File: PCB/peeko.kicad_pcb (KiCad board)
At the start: 2 copper layers, 21.8 x 51.3 mm, 6 parts, among them J1 Rasberry PI Pico, J2 Conn_02x15_Odd_Even, J3 Conn_01x02_Pin, J4 Conn_01x02_Pin

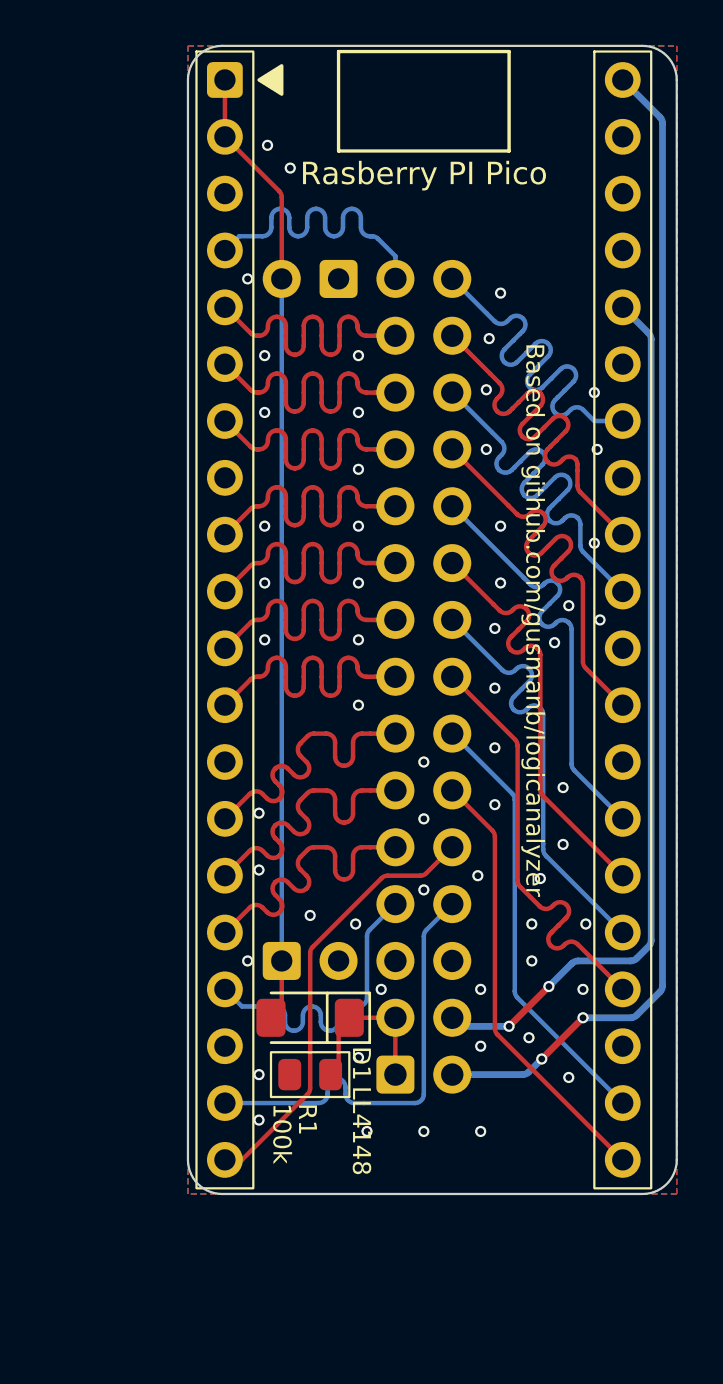
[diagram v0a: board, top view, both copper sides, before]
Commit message: schematic for JY board, remove all but PCBs
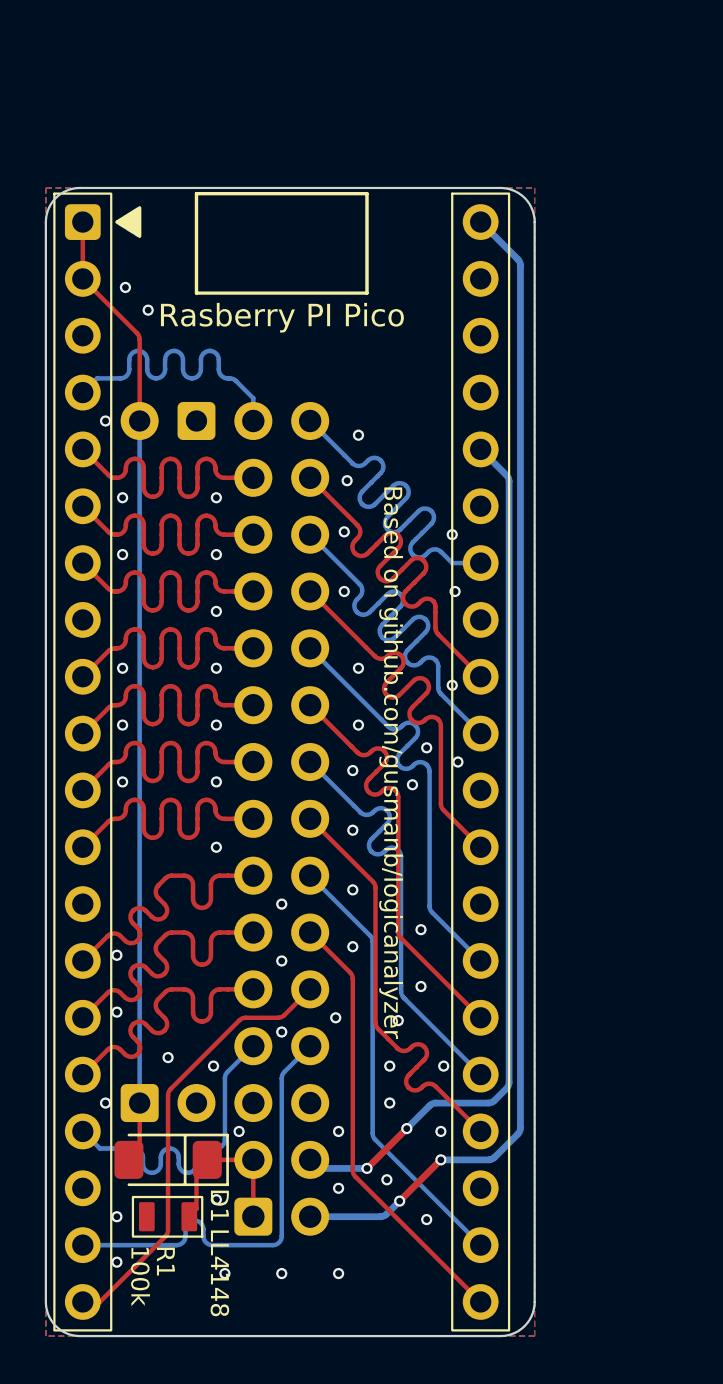
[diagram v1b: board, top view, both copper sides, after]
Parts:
- moved D1 8.98 mm to (147.3, 125.7)
- moved J1 8.98 mm to (152.4, 108.0)
- moved J2 8.98 mm to (151.1, 128.3)
- moved R1 8.98 mm to (147.3, 128.3)
- moved J3 8.98 mm to (146.1, 123.2)
- moved J4 8.98 mm to (148.6, 92.7)
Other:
- board text added: "14.55 19.63"
- board text added: "Traces going to the odd row of the IDC connector are 5.08mm shorter to account for the longer pins in the connector."
- board text removed: "14.55mm 19.63mm"
- board text removed: "The pins in the odd row of the horizontal IDC connector are 5.08mm longer, so the traces going to those pins are 5.08mm shorter."

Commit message: fixup local symbols, footprints, models, move power traces inboard
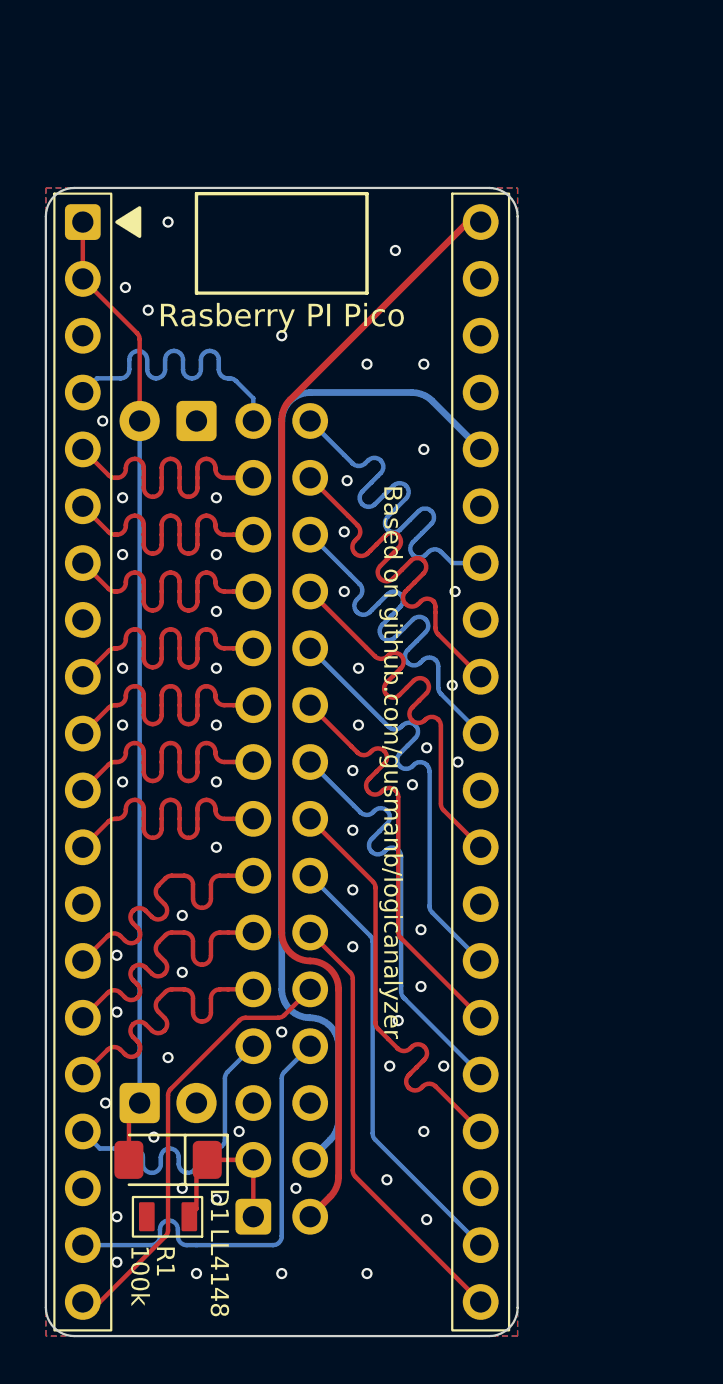
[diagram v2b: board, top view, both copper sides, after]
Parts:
- J2: footprint Connector_IDC:IDC-Header_2x15_P2.54mm_Horizontal -> 000_LOCAL:IDC-Header_2x15_P2.54mm_Horizontal
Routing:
- net +3V3: track 39.5 -> 45.4 mm, vias 2 -> 0
- net +5V: track 52.3 -> 50.2 mm, vias 2 -> 0
- net GND: vias 58 -> 60
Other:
- board size 21.8 x 51.3 mm -> 21.1 x 51.3 mm
